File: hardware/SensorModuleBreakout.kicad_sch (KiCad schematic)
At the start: 34 parts, among them J1 Conn_ST_STDC14, J2 Conn_01x10, J3 Conn_01x15, J4 Conn_01x03, J5 Conn_01x04, U1 STM32U031C8Tx, U2 SHT4x, U3 STC31-C-R3, U5 MS5607-02BA

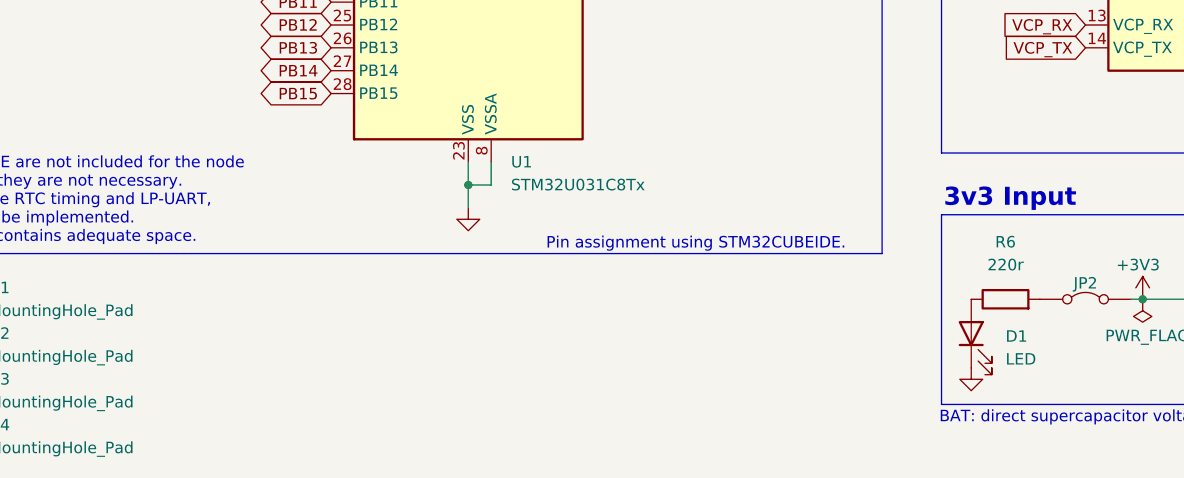
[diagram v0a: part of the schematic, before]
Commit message: add comment on MCU choice
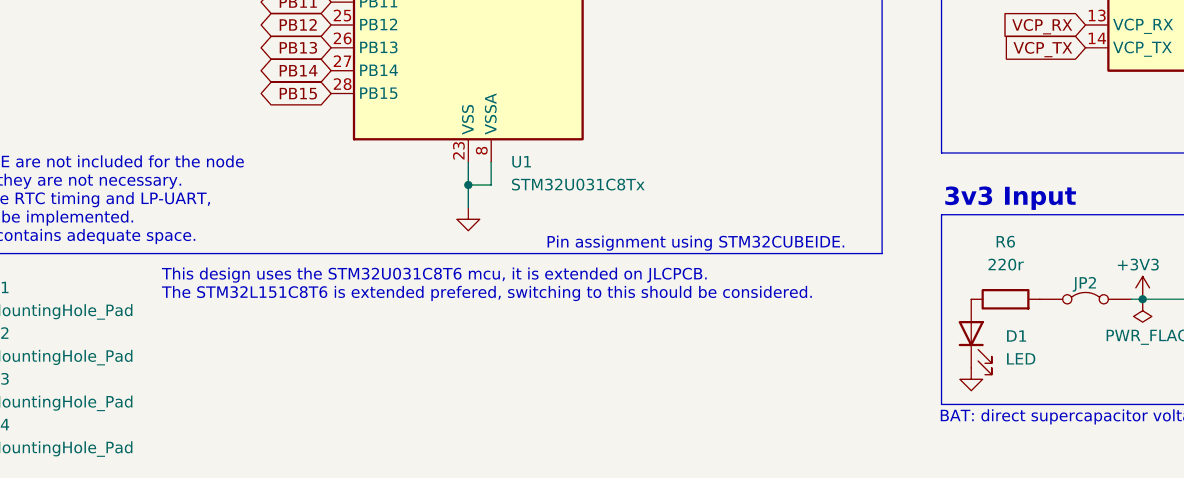
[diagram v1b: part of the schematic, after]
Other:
- note added: "This design uses the STM32U031C8T6 mcu, it is extended on JLCPCB. The STM32L151C8T6 is extended prefered, switching to this should be considered."
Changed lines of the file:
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@@
+		)
+	)
+	(text "This design uses the STM32U031C8T6 mcu, it is extended on JLCPCB.\nThe STM32L151C8T6 is extended prefered, switching to this should be considered."
+		(exclude_from_sim no)
+		(at 47.244 139.446 0)
+		(effects
+			(font
+				(size 1.27 1.27)
+			)
+			(justify left)
 		)
 	)
